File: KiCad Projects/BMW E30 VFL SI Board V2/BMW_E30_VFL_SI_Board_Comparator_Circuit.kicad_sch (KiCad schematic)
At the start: 39 parts, among them K1 SR7-9V-200-1C, Q1 BC547C, U2 LM2901

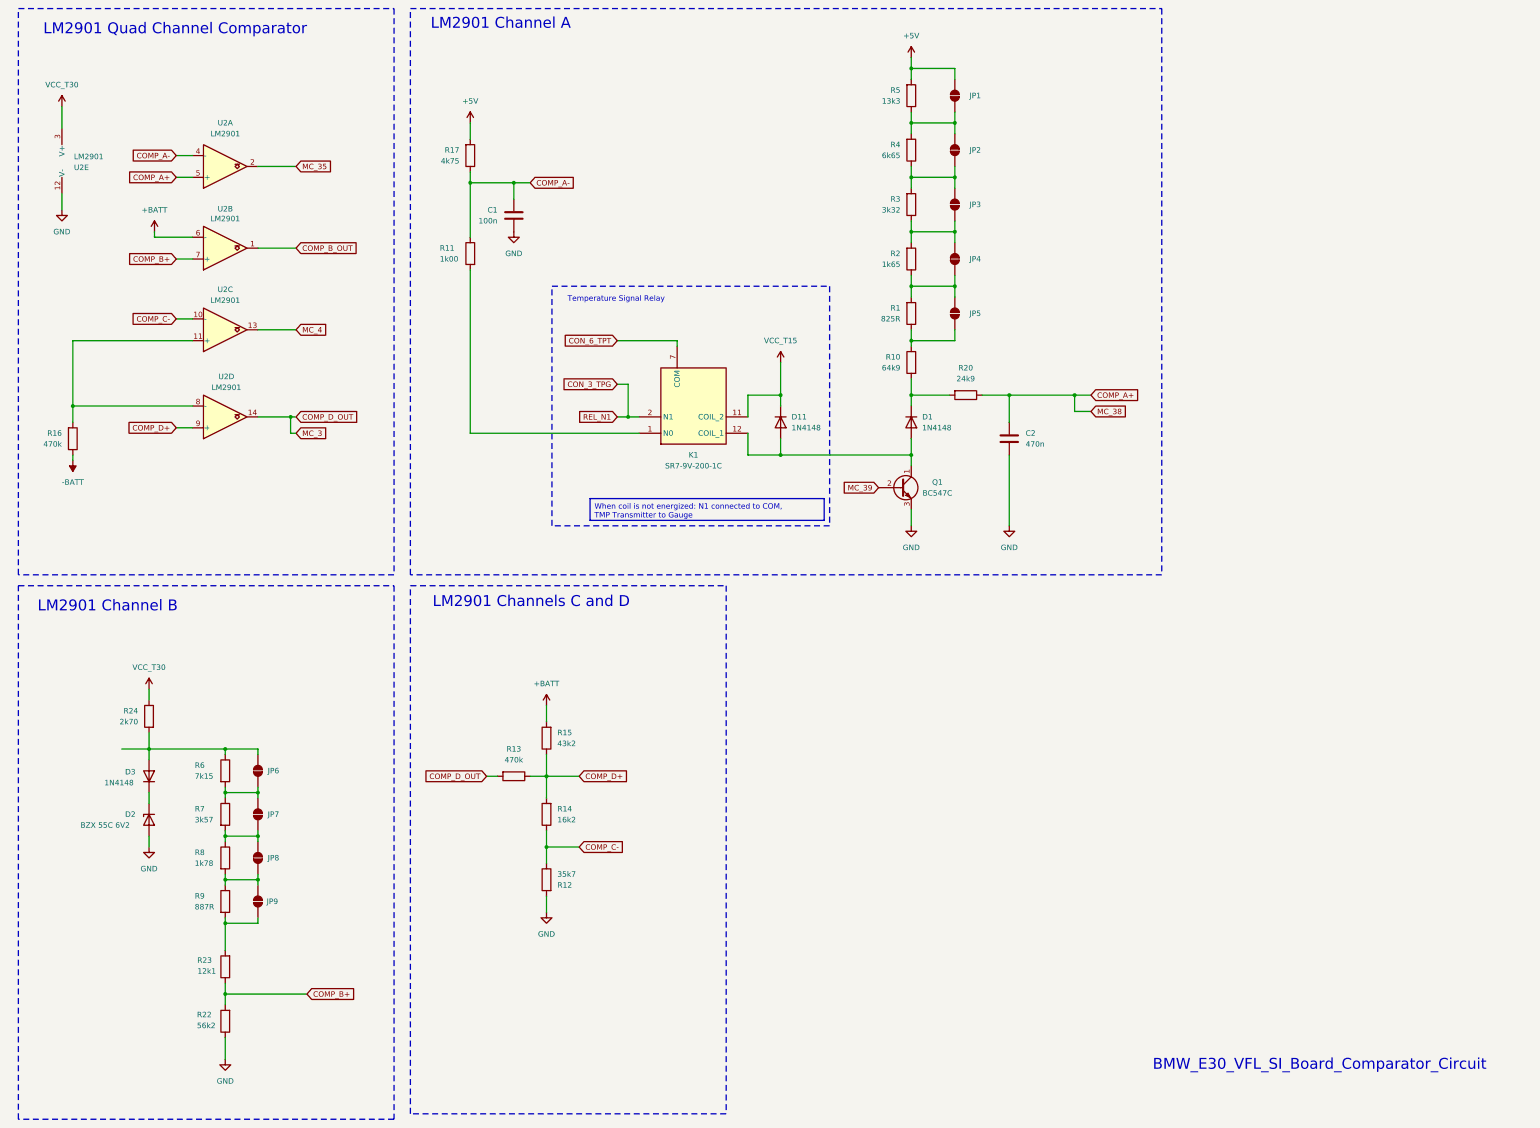
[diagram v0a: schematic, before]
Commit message: V2 Board Updates
Added in extra resistors, cap, and diode that were added to a  particular version of the SI board from the USDM on the comparator circuit. Updated the schematic diagram of the comparator circuit to improve readability. Updated the clock frequency measured with a scope. Made a few minor layout improvements including moving the "JP" connections inwards as not to interfere with the plastic housing for the PCB in the cluster and other minor layout errors such as swapped reference designators. Updated info on where the +5V regulator gets its source voltage from. These updates are reflected in schematic version V2.1 as denoted in the title box (not in the title of the schematic file).
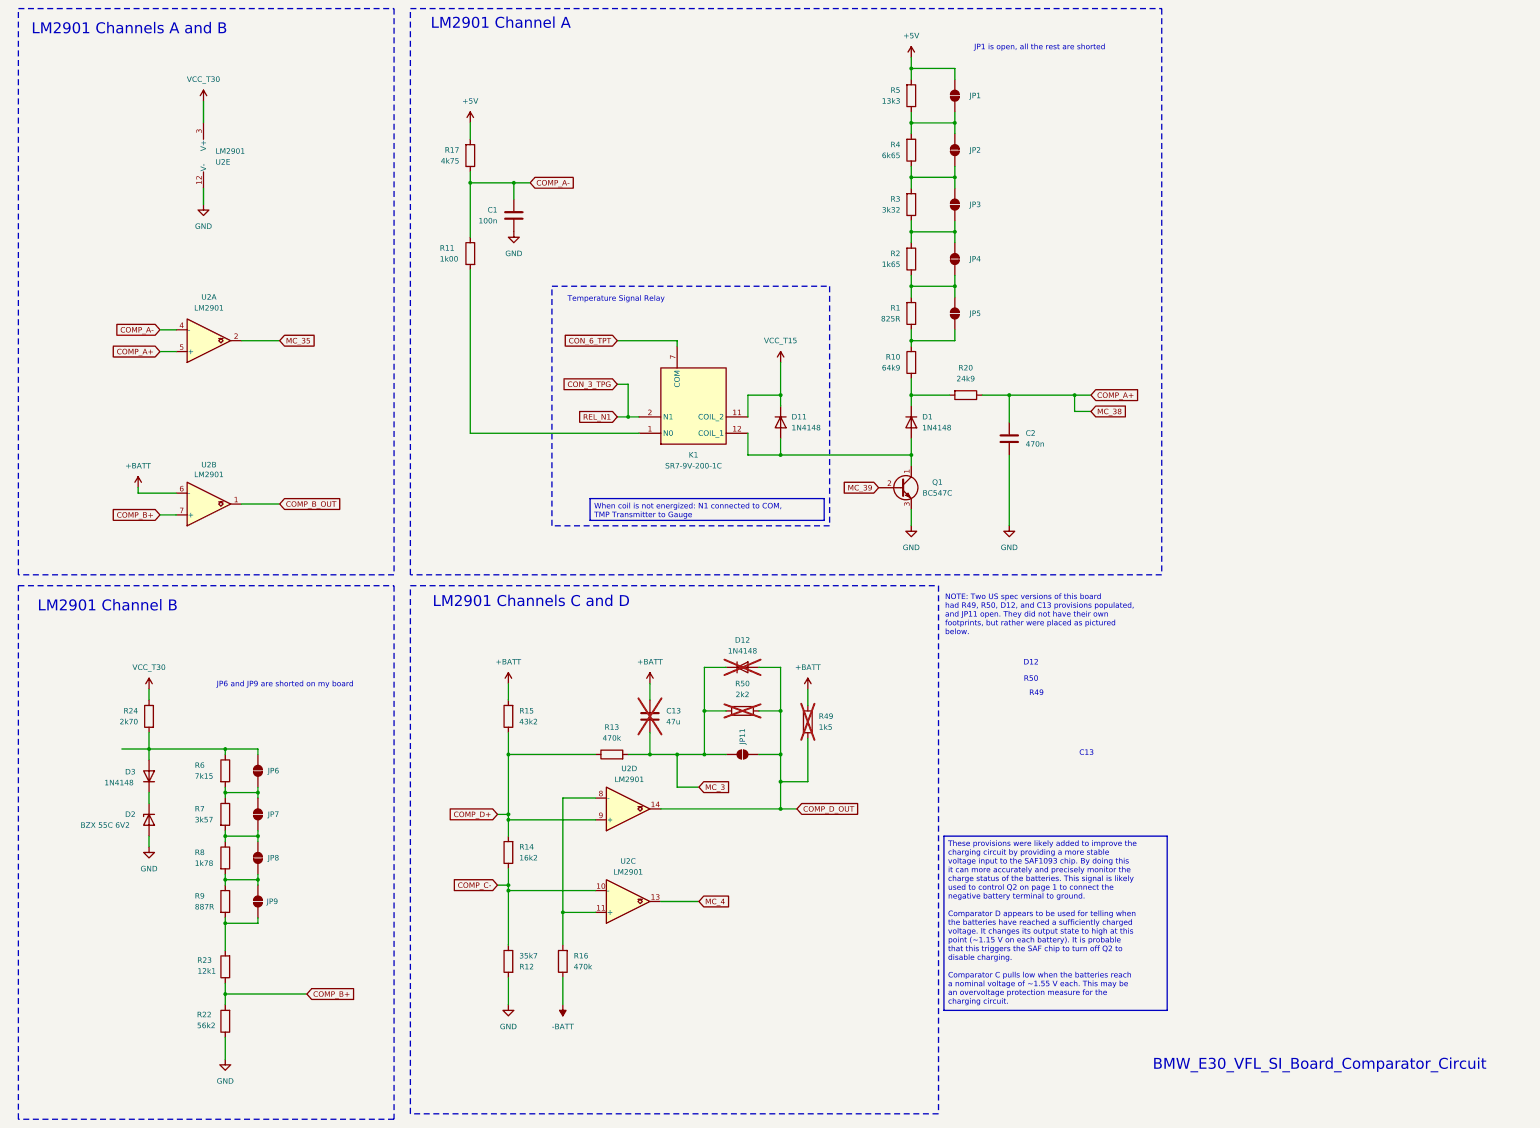
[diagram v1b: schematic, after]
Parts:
- added C13: 47u, symbol Device:C
- added D12: 1N4148, symbol Diode:1N4148
- added JP11: SolderJumper_2_Open, Jumper:SolderJumper-2_P1.3mm_Open_Pad1.0x1.5mm, symbol Jumper:SolderJumper_2_Open
- added R49: 1k5, symbol Device:R
- added R50: 2k2, symbol Device:R
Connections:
- net +BATT: now also C13.2, R49.2
- net COMP_D_OUT: now also D12.2 (A), JP11.2 (B), R49.1, R50.1; no longer R13.2
- new net MC_3: C13.1, D12.1 (K), JP11.1 (A), R13.2, R50.2
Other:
- note added: "C13"
- note added: "D12"
- note added: "JP1 is open, all the rest are shorted"
- note added: "JP6 and JP9 are shorted on my board"
- note added: "LM2901 Channels A and B"
- note added: "NOTE: Two US spec versions of this board had R49, R50, D12, and C13 provisions populated, and JP11 open. They did not have their own footprints, but rather were placed as pictured below."
- note added: "R49"
- note added: "R50"
- note removed: "LM2901 Quad Channel Comparator"
- moved on the sheet: R12, R13, R14, R15, R16, U2A, U2B, U2C, U2D, U2E
